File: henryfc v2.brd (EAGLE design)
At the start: 30 x 30 mm, 74 parts, among them X1 SM07B-SRSS-TB

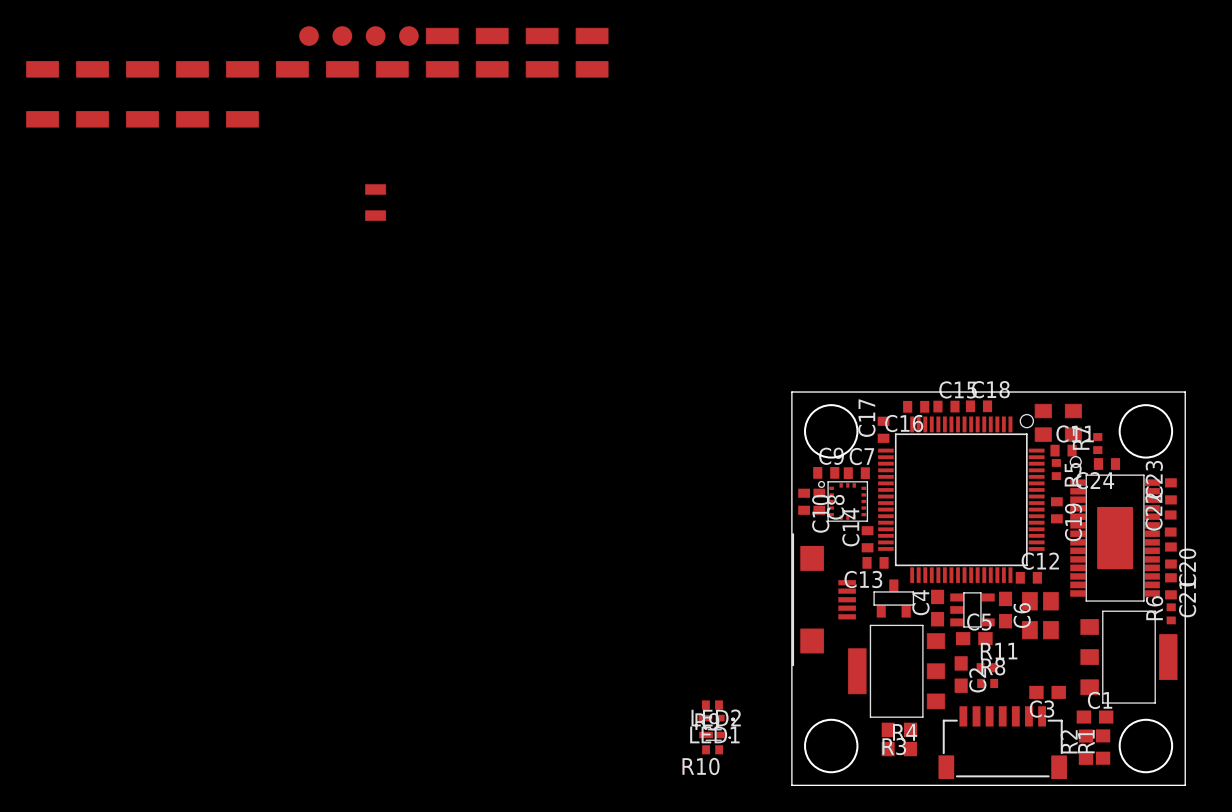
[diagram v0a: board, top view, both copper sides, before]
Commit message: updating pcb
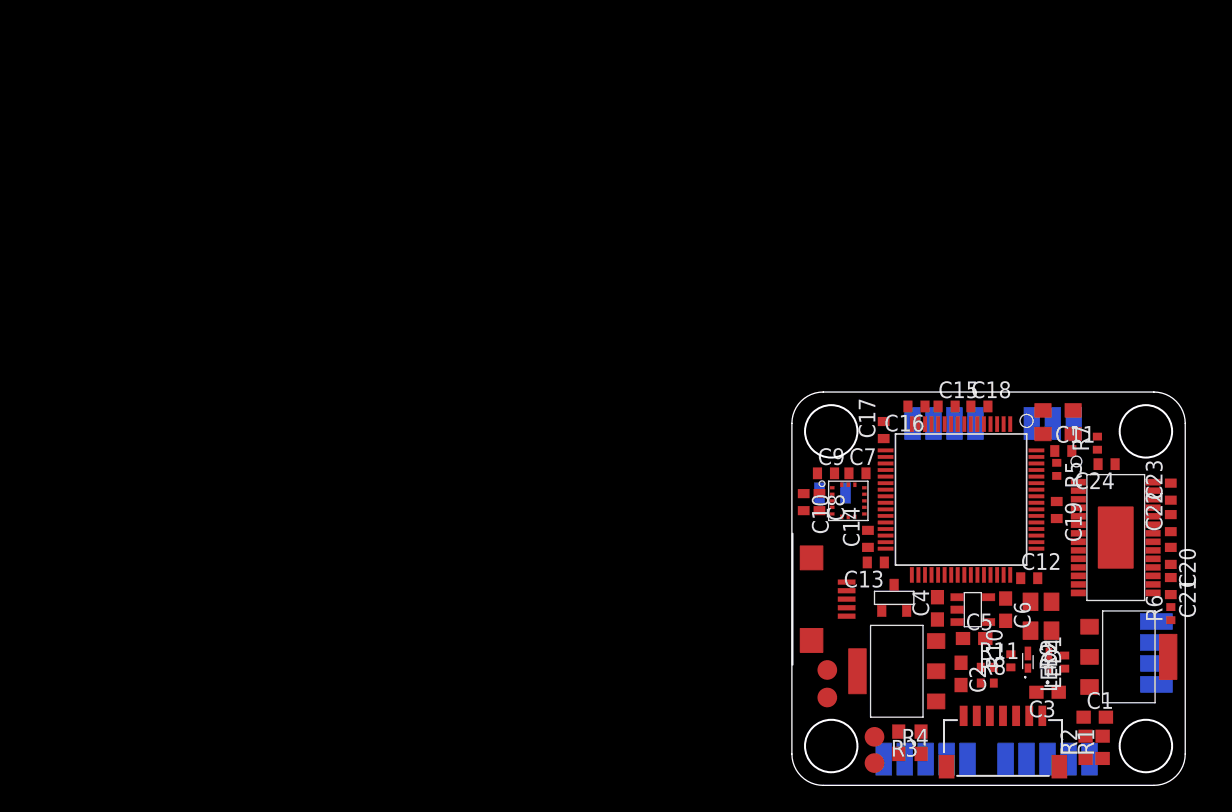
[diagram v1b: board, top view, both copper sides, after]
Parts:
- moved U$32 90.3 mm to (16.3, 2.00), flipped to the bottom, turned to 270 degrees
- moved U$19 89.7 mm to (27.8, 12.5), flipped to the bottom
- moved U$29 86.3 mm to (22.7, 2.00), flipped to the bottom, turned to 270 degrees
- moved U$30 85.5 mm to (17.9, 2.00), flipped to the bottom, turned to 270 degrees
- moved U$20 83.2 mm to (10.2, 2.00), flipped to the bottom, turned to 270 degrees
- moved U$14 82.7 mm to (21.1, 2.00), flipped to the bottom, turned to 270 degrees
- moved U$31 79.6 mm to (21.5, 27.6), flipped to the bottom, turned to 270 degrees
- moved U$36 73.6 mm to (27.8, 7.70), flipped to the bottom, turned to 180 degrees
- moved TP3 68.7 mm to (6.30, 1.70), turned to 180 degrees
- moved U$25 67.5 mm to (11.8, 2.00), flipped to the bottom, turned to 270 degrees
- moved U$34 67.0 mm to (27.8, 9.30), flipped to the bottom
- moved U$13 64.5 mm to (18.3, 27.6), flipped to the bottom, turned to 270 degrees
- moved TP1 64.2 mm to (6.30, 3.70)
- moved TP4 64.1 mm to (2.70, 6.70)
- moved U$23 63.9 mm to (13.4, 2.00), flipped to the bottom, turned to 270 degrees
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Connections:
- net CLKIN renamed OSD_N
- net OSC_IN renamed F7_P
- net OSC_OUT renamed F7_N
- net OTG_FS_DM renamed USBDATA_N
- net OTG_FS_DP renamed USBDATA_P
- net XFB renamed OSD_P
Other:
- outline, holes or cut-outs redrawn
- board text added: "RX"
- board text added: "VTX"
- board text added: "cam"
